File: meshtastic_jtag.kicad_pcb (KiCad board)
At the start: 2 copper layers, 120 x 50 mm, 19 parts, among them J2 JTAG, J4 usr_btn, J5 pcb antenna, U1 ESP32-DevKitC, U2 E22-900M22S, U3 OLED, U4 neo6m

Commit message: schematic pdf and gerbers added
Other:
- board text added: "JLCJLCJLCJLC"
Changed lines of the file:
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@@
   (general
     (thickness 1.6)
-    (drawings 16)
+    (drawings 17)
     (tracks 536)
     (zones 0)
@@
     (visible_elements FFFFFF7F)
     (pcbplotparams
-      (layerselection 0x010fc_ffffffff)
-      (usegerberextensions false)
-      (usegerberattributes true)
-      (usegerberadvancedattributes true)
-      (creategerberjobfile true)
+      (layerselection 0x010f0_ffffffff)
+      (usegerberextensions true)
+      (usegerberattributes false)
+      (usegerberadvancedattributes false)
+      (creategerberjobfile false)
       (excludeedgelayer true)
       (linewidth 0.100000)
@@
       (psa4output false)
       (plotreference true)
-      (plotvalue true)
+      (plotvalue false)
       (plotinvisibletext false)
       (padsonsilk false)
-      (subtractmaskfromsilk false)
+      (subtractmaskfromsilk true)
       (outputformat 1)
       (mirror false)
-      (drillshape 1)
+      (drillshape 0)
       (scaleselection 1)
-      (outputdirectory ""))
+      (outputdirectory "gerber/"))
   )
   (net 0 "")
@@
       (effects (font (size 1 1) (thickness 0.15)))
     )
-    (fp_text user SDA (at 3.81 2.8 unlocked) (layer F.SilkS)
-      (effects (font (size 1 1) (thickness 0.2)))
-    )
-    (fp_text user SCL (at 1.27 2.8 unlocked) (layer F.SilkS)
-      (effects (font (size 1 1) (thickness 0.2)))
-    )
-    (fp_text user GND (at -1.27 2.8 unlocked) (layer F.SilkS)
-      (effects (font (size 1 1) (thickness 0.2)))
-    )
-    (fp_text user VCC (at -3.8 2.8 unlocked) (layer F.SilkS)
-      (effects (font (size 1 1) (thickness 0.2)))
-    )
     (fp_line (start 13.5 -1.7) (end 13.5 25.3) (layer F.CrtYd) (width 0.12))
     (fp_line (start 13.5 25.3) (end -13.5 25.3) (layer F.CrtYd) (width 0.12))
@@
     (fp_line (start -13.7 25.5) (end -8.7 25.5) (layer F.SilkS) (width 0.2))
     (fp_line (start -13.7 25.5) (end -13.7 20.5) (layer F.SilkS) (width 0.2))
+    (fp_text user SDA (at 3.81 2.8 unlocked) (layer F.SilkS)
+      (effects (font (size 1 1) (thickness 0.2)))
+    )
+    (fp_text user SCL (at 1.27 2.8 unlocked) (layer F.SilkS)
+      (effects (font (size 1 1) (thickness 0.2)))
+    )
+    (fp_text user GND (at -1.27 2.8 unlocked) (layer F.SilkS)
+      (effects (font (size 1 1) (thickness 0.2)))
+    )
+    (fp_text user VCC (at -3.8 2.8 unlocked) (layer F.SilkS)
+      (effects (font (size 1 1) (thickness 0.2)))
+    )
     (pad 4 thru_hole circle (at 3.81 0 270) (size 1.7 1.7) (drill 1) (layers *.Cu *.Mask)
       (net 21 /SDA))
@@
       (effects (font (size 1 1) (thickness 0.15)))
     )
-    (fp_text user %R (at 0 0) (layer F.Fab)
-      (effects (font (size 0.5 0.5) (thickness 0.08)))
-    )
     (fp_line (start -1 0.625) (end -1 -0.625) (layer F.Fab) (width 0.1))
     (fp_line (start -1 -0.625) (end 1 -0.625) (layer F.Fab) (width 0.1))
@@
     (fp_line (start 1.68 -0.95) (end 1.68 0.95) (layer F.CrtYd) (width 0.05))
     (fp_line (start 1.68 0.95) (end -1.68 0.95) (layer F.CrtYd) (width 0.05))
-    (pad 2 smd roundrect (at 0.9125 0) (size 1.025 1.4) (layers F.Cu F.Paste F.Mask) (roundrect_rratio 0.243902)
+    (fp_text user %R (at 0 0) (layer F.Fab)
+      (effects (font (size 0.5 0.5) (thickness 0.08)))
+    )
+    (pad 2 smd roundrect (at 0.9125 0) (size 1.025 1.4) (layers F.Cu F.Paste F.Mask) (roundrect_rratio 0.2439004878048781)
       (net 38 +3V3))
-    (pad 1 smd roundrect (at -0.9125 0) (size 1.025 1.4) (layers F.Cu F.Paste F.Mask) (roundrect_rratio 0.243902)
+    (pad 1 smd roundrect (at -0.9125 0) (size 1.025 1.4) (layers F.Cu F.Paste F.Mask) (roundrect_rratio 0.2439004878048781)
       (net 37 /usr_btn))
     (model ${KISYS3DMOD}/Resistor_SMD.3dshapes/R_0805_2012Metric.wrl
@@
     (fp_text value 1k (at 0 1.65) (layer F.Fab)
       (effects (font (size 1 1) (thickness 0.15)))
-    )
-    (fp_text user %R (at 0 0) (layer F.Fab)
-      (effects (font (size 0.5 0.5) (thickness 0.08)))
     )
     (fp_line (start -1 0.625) (end -1 -0.625) (layer F.Fab) (width 0.1))
@@
     (fp_line (start 1.68 -0.95) (end 1.68 0.95) (layer F.CrtYd) (width 0.05))
     (fp_line (start 1.68 0.95) (end -1.68 0.95) (layer F.CrtYd) (width 0.05))
-    (pad 2 smd roundrect (at 0.9125 0) (size 1.025 1.4) (layers F.Cu F.Paste F.Mask) (roundrect_rratio 0.243902)
+    (fp_text user %R (at 0 0) (layer F.Fab)
+      (effects (font (size 0.5 0.5) (thickness 0.08)))
+    )
+    (pad 2 smd roundrect (at 0.9125 0) (size 1.025 1.4) (layers F.Cu F.Paste F.Mask) (roundrect_rratio 0.2439004878048781)
       (net 42 "Net-(R2-Pad2)"))
-    (pad 1 smd roundrect (at -0.9125 0) (size 1.025 1.4) (layers F.Cu F.Paste F.Mask) (roundrect_rratio 0.243902)
+    (pad 1 smd roundrect (at -0.9125 0) (size 1.025 1.4) (layers F.Cu F.Paste F.Mask) (roundrect_rratio 0.2439004878048781)
       (net 41 "Net-(D1-Pad2)"))
     (model ${KISYS3DMOD}/Resistor_SMD.3dshapes/R_0805_2012Metric.wrl
@@
     (fp_text value LED (at 0 1.65) (layer F.Fab)
       (effects (font (size 1 1) (thickness 0.15)))
-    )
-    (fp_text user %R (at 0 0) (layer F.Fab)
-      (effects (font (size 0.5 0.5) (thickness 0.08)))
     )
     (fp_line (start 1 -0.6) (end -0.7 -0.6) (layer F.Fab) (width 0.1))
@@
     (fp_line (start 1.68 -0.95) (end 1.68 0.95) (layer F.CrtYd) (width 0.05))
     (fp_line (start 1.68 0.95) (end -1.68 0.95) (layer F.CrtYd) (width 0.05))
+    (fp_text user %R (at 0 0) (layer F.Fab)
+      (effects (font (size 0.5 0.5) (thickness 0.08)))
+    )
     (pad 2 smd roundrect (at 0.9375 0) (size 0.975 1.4) (layers F.Cu F.Paste F.Mask) (roundrect_rratio 0.25)
       (net 41 "Net-(D1-Pad2)"))
@@
     )
   )
+  (gr_text JLCJLCJLCJLC (at 125.4 100.7 270) (layer B.SilkS)
+    (effects (font (size 1 1) (thickness 0.15)) (justify mirror))
+  )
   (gr_text "Meshtastic JTAG \ndevboard V1.0" (at 168.1 118.5) (layer F.SilkS)

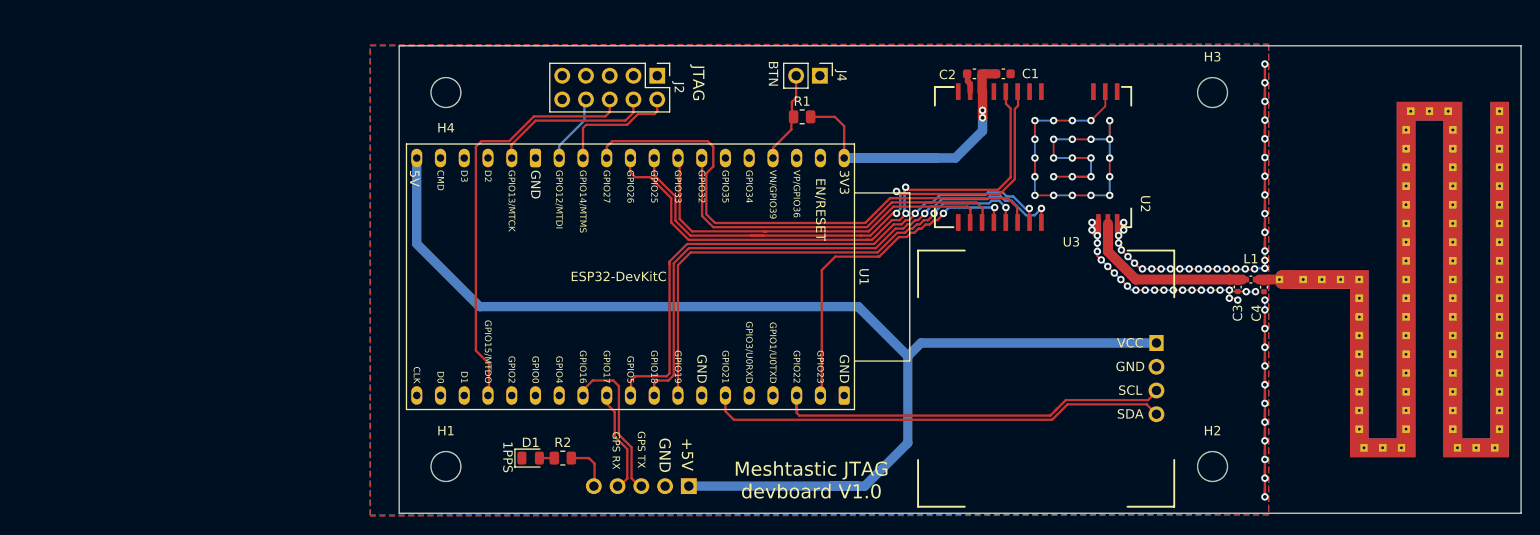
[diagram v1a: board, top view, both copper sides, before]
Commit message: bump to V1.1, solder jumpers to swap OLED VCC/GND added
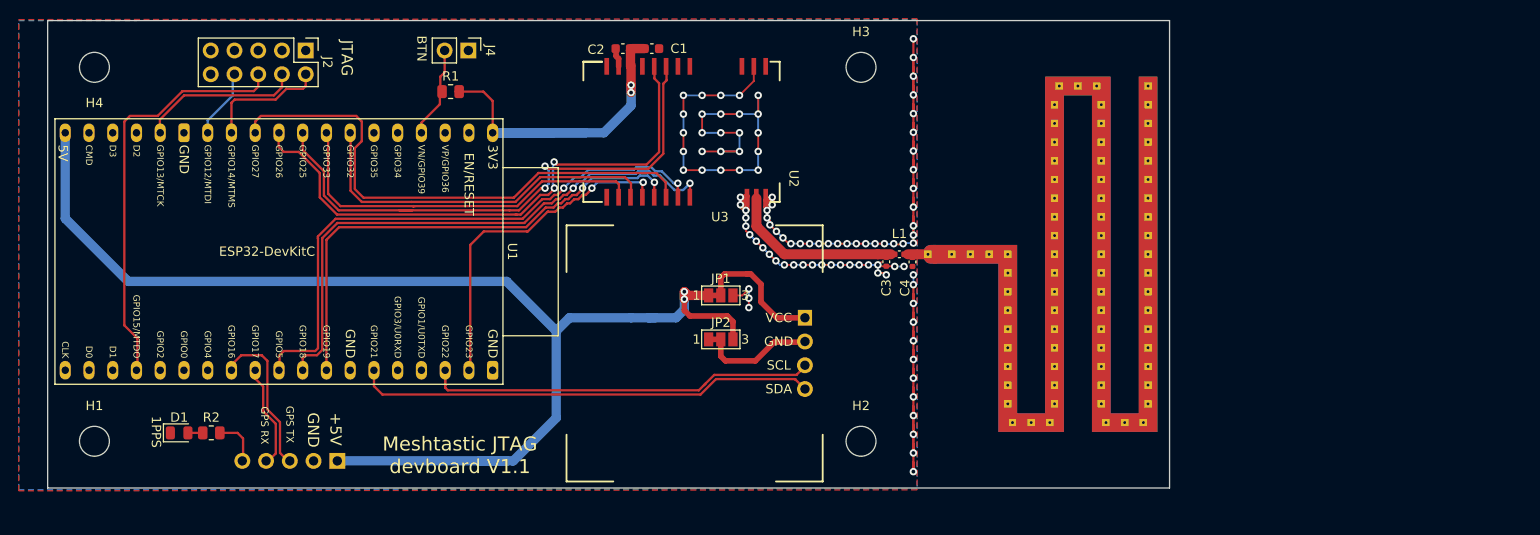
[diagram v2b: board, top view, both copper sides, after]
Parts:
- added JP1: jumper, Jumper:SolderJumper-3_P1.3mm_Bridged12_Pad1.0x1.5mm_NumberLabels, F.Cu at (158.4, 98.7)
- added JP2: jumper, Jumper:SolderJumper-3_P1.3mm_Bridged12_Pad1.0x1.5mm_NumberLabels, F.Cu at (158.4, 103.4)
- moved U2 37.7 mm to (154.2, 81.2)
- moved U4 37.7 mm to (112.3, 116.4)
- moved C1 37.7 mm to (151.0, 72.3)
- moved C2 37.7 mm to (147.9, 72.3)
- moved C3 37.7 mm to (176.1, 95.1)
- moved C4 37.7 mm to (178.9, 95.1)
- moved D1 37.7 mm to (100.5, 113.4)
- moved H1 37.7 mm to (91.4, 114.3)
- moved H2 37.7 mm to (173.4, 114.3)
- moved H3 37.7 mm to (173.4, 74.3)
- moved H4 37.7 mm to (91.4, 74.3)
- moved J2 37.7 mm to (114.0, 72.5)
- moved J4 37.7 mm to (131.4, 72.5)
- moved J5 37.7 mm to (203.1, 75.3)
- moved L1 37.7 mm to (177.5, 94.3)
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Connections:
- U3 pad 1: +5V -> Net-(JP1-Pad2)
- U3 pad 2: GND -> Net-(JP2-Pad2)
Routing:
- net Net-(JP1-Pad2): track 0.00 -> 14.1 mm
- net Net-(JP2-Pad2): track 0.00 -> 12.0 mm
- net GND: track 184.4 -> 188.3 mm, vias 95 -> 98
- net +5V: track 131.4 -> 133.8 mm, vias 0 -> 2
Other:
- board text added: "Meshtastic JTAG devboard V1.1"
- board text removed: "Meshtastic JTAG devboard V1.0"
